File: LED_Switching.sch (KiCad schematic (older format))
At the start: 13 parts

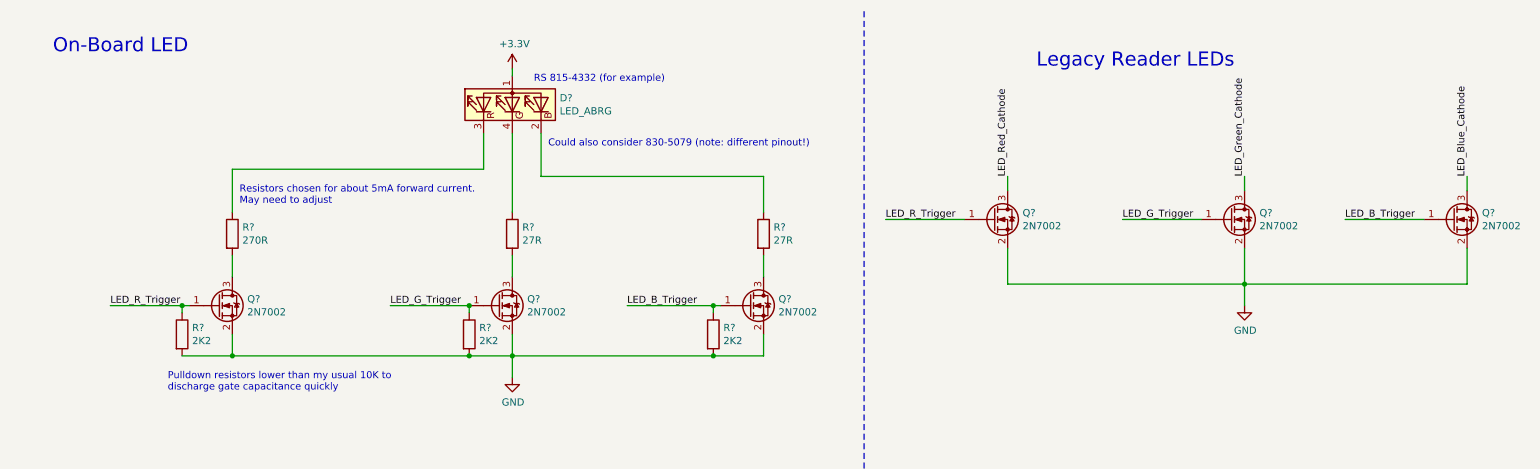
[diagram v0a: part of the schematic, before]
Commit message: Annotated some symbols and linked nets properly between sheets
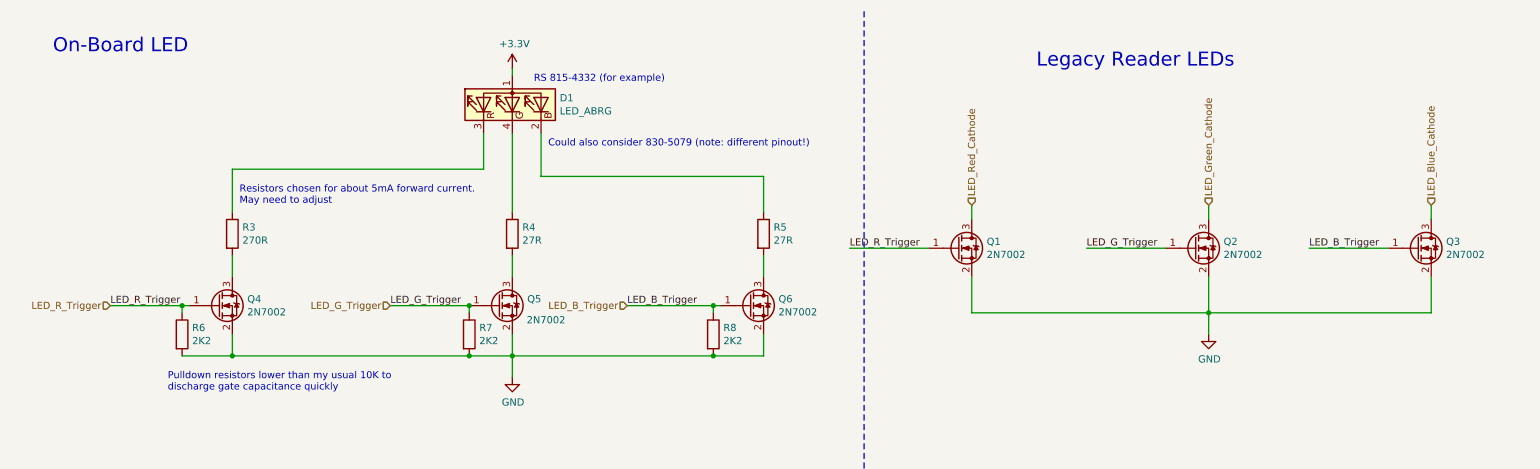
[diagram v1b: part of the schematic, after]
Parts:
- R3, R4, R5, R6, R7, R8: renamed from R?; footprint (none) -> Resistor_SMD:R_0603_1608Metric
- gave numbers to parts that had none: 7
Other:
- moved on the sheet: Q1, Q2, Q3
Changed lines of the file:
@@
 P 4050 1150
 AR Path="/5FDB67B7" Ref="D?"  Part="1"
-AR Path="/5FDAF572/5FDB67B7" Ref="D?"  Part="1"
-F 0 "D?" V 4096 820 50  0000 R CNN
+AR Path="/5FDAF572/5FDB67B7" Ref="D1"  Part="1"
+F 0 "D1" V 4096 820 50  0000 R CNN
 F 1 "LED_ABRG" V 4005 820 50  0000 R CNN
 F 2 "" H 4050 1150 50  0001 C CNN
@@
 P 4050 2050
 AR Path="/5FDCD5C9" Ref="R?"  Part="1"
-AR Path="/5FDAF572/5FDCD5C9" Ref="R?"  Part="1"
-F 0 "R?" H 4120 2096 50  0000 L CNN
+AR Path="/5FDAF572/5FDCD5C9" Ref="R4"  Part="1"
+F 0 "R4" H 4120 2096 50  0000 L CNN
 F 1 "27R" H 4120 2005 50  0000 L CNN
-F 2 "" V 3980 2050 50  0001 C CNN
+F 2 "Resistor_SMD:R_0603_1608Metric" V 3980 2050 50  0001 C CNN
 F 3 "~" H 4050 2050 50  0001 C CNN
 	1    4050 2050
@@
 P 3950 2550
 AR Path="/5FDCD5CF" Ref="Q?"  Part="1"
-AR Path="/5FDAF572/5FDCD5CF" Ref="Q?"  Part="1"
-F 0 "Q?" H 4154 2596 50  0000 L CNN
-F 1 "2N7002" H 4154 2505 50  0000 L CNN
+AR Path="/5FDAF572/5FDCD5CF" Ref="Q5"  Part="1"
+F 0 "Q5" H 4154 2596 50  0000 L CNN
+F 1 "2N7002" H 4150 2450 50  0000 L CNN
 F 2 "Package_TO_SOT_SMD:SOT-23" H 4150 2475 50  0001 L CIN
 F 3 "https://www.fairchildsemi.com/datasheets/2N/2N7002.pdf" H 3950 2550 50  0001 L CNN
@@
 P 5800 2050
 AR Path="/5FDCEFE5" Ref="R?"  Part="1"
-AR Path="/5FDAF572/5FDCEFE5" Ref="R?"  Part="1"
-F 0 "R?" H 5870 2096 50  0000 L CNN
+AR Path="/5FDAF572/5FDCEFE5" Ref="R5"  Part="1"
+F 0 "R5" H 5870 2096 50  0000 L CNN
 F 1 "27R" H 5870 2005 50  0000 L CNN
-F 2 "" V 5730 2050 50  0001 C CNN
+F 2 "Resistor_SMD:R_0603_1608Metric" V 5730 2050 50  0001 C CNN
 F 3 "~" H 5800 2050 50  0001 C CNN
 	1    5800 2050
@@
 P 5700 2550
 AR Path="/5FDCEFEB" Ref="Q?"  Part="1"
-AR Path="/5FDAF572/5FDCEFEB" Ref="Q?"  Part="1"
-F 0 "Q?" H 5904 2596 50  0000 L CNN
+AR Path="/5FDAF572/5FDCEFEB" Ref="Q6"  Part="1"
+F 0 "Q6" H 5904 2596 50  0000 L CNN
 F 1 "2N7002" H 5904 2505 50  0000 L CNN
 F 2 "Package_TO_SOT_SMD:SOT-23" H 5900 2475 50  0001 L CIN
@@
 	5800 2750 5800 2900
 $Comp
-L Transistor_FET:2N7002 Q?
+L Transistor_FET:2N7002 Q1
 U 1 1 5FDFC391
-P 7400 1950
-F 0 "Q?" H 7604 1996 50  0000 L CNN
-F 1 "2N7002" H 7604 1905 50  0000 L CNN
-F 2 "Package_TO_SOT_SMD:SOT-23" H 7600 1875 50  0001 L CIN
-F 3 "https://www.fairchildsemi.com/datasheets/2N/2N7002.pdf" H 7400 1950 50  0001 L CNN
-	1    7400 1950
-	1    0    0    -1
-$EndComp
-$Comp
-L Transistor_FET:2N7002 Q?
+P 7150 2150
+F 0 "Q1" H 7354 2196 50  0000 L CNN
+F 1 "2N7002" H 7354 2105 50  0000 L CNN
+F 2 "Package_TO_SOT_SMD:SOT-23" H 7350 2075 50  0001 L CIN
+F 3 "https://www.fairchildsemi.com/datasheets/2N/2N7002.pdf" H 7150 2150 50  0001 L CNN
+	1    7150 2150
+	1    0    0    -1
+$EndComp
+$Comp
+L Transistor_FET:2N7002 Q2
 U 1 1 5FDFF38B
-P 9050 1950
-F 0 "Q?" H 9254 1996 50  0000 L CNN
-F 1 "2N7002" H 9254 1905 50  0000 L CNN
-F 2 "Package_TO_SOT_SMD:SOT-23" H 9250 1875 50  0001 L CIN
-F 3 "https://www.fairchildsemi.com/datasheets/2N/2N7002.pdf" H 9050 1950 50  0001 L CNN
-	1    9050 1950
-	1    0    0    -1
-$EndComp
-$Comp
-L Transistor_FET:2N7002 Q?
+P 8800 2150
+F 0 "Q2" H 9004 2196 50  0000 L CNN
+F 1 "2N7002" H 9004 2105 50  0000 L CNN
+F 2 "Package_TO_SOT_SMD:SOT-23" H 9000 2075 50  0001 L CIN
+F 3 "https://www.fairchildsemi.com/datasheets/2N/2N7002.pdf" H 8800 2150 50  0001 L CNN
+	1    8800 2150
+	1    0    0    -1
+$EndComp
+$Comp
+L Transistor_FET:2N7002 Q3
 U 1 1 5FE04D0B
-P 10600 1950
-F 0 "Q?" H 10804 1996 50  0000 L CNN
-F 1 "2N7002" H 10804 1905 50  0000 L CNN
-F 2 "Package_TO_SOT_SMD:SOT-23" H 10800 1875 50  0001 L CIN
-F 3 "https://www.fairchildsemi.com/datasheets/2N/2N7002.pdf" H 10600 1950 50  0001 L CNN
-	1    10600 1950
+P 10350 2150
+F 0 "Q3" H 10554 2196 50  0000 L CNN
+F 1 "2N7002" H 10554 2105 50  0000 L CNN
+F 2 "Package_TO_SOT_SMD:SOT-23" H 10550 2075 50  0001 L CIN
+F 3 "https://www.fairchildsemi.com/datasheets/2N/2N7002.pdf" H 10350 2150 50  0001 L CNN
+	1    10350 2150
 	1    0    0    -1
 $EndComp
@@
 L power:GND #PWR0121
 U 1 1 5FE094F3
-P 9150 2550
-F 0 "#PWR0121" H 9150 2300 50  0001 C CNN
-F 1 "GND" H 9155 2377 50  0000 C CNN
-F 2 "" H 9150 2550 50  0001 C CNN
-F 3 "" H 9150 2550 50  0001 C CNN
-	1    9150 2550
+P 8900 2750
+F 0 "#PWR0121" H 8900 2500 50  0001 C CNN
+F 1 "GND" H 8905 2577 50  0000 C CNN
+F 2 "" H 8900 2750 50  0001 C CNN
+F 3 "" H 8900 2750 50  0001 C CNN
+	1    8900 2750
 	1    0    0    -1
 $EndComp
@@
 Legacy Reader LEDs
 Wire Wire Line
-	7500 2150 7500 2400
-Wire Wire Line
-	10700 2400 10700 2150
+	7250 2350 7250 2600
+Wire Wire Line
+	10450 2600 10450 2350
 Wire Wire Line
 	2100 2750 2100 2900
@@
 P 2000 2550
 AR Path="/5FDB67DA" Ref="Q?"  Part="1"
-AR Path="/5FDAF572/5FDB67DA" Ref="Q?"  Part="1"
-F 0 "Q?" H 2204 2596 50  0000 L CNN
+AR Path="/5FDAF572/5FDB67DA" Ref="Q4"  Part="1"
+F 0 "Q4" H 2204 2596 50  0000 L CNN
 F 1 "2N7002" H 2204 2505 50  0000 L CNN
 F 2 "Package_TO_SOT_SMD:SOT-23" H 2200 2475 50  0001 L CIN
@@
 P 2100 2050
 AR Path="/5FDB67BE" Ref="R?"  Part="1"
-AR Path="/5FDAF572/5FDB67BE" Ref="R?"  Part="1"
-F 0 "R?" H 2170 2096 50  0000 L CNN
+AR Path="/5FDAF572/5FDB67BE" Ref="R3"  Part="1"
+F 0 "R3" H 2170 2096 50  0000 L CNN
 F 1 "270R" H 2170 2005 50  0000 L CNN
-F 2 "" V 2030 2050 50  0001 C CNN
+F 2 "Resistor_SMD:R_0603_1608Metric" V 2030 2050 50  0001 C CNN
 F 3 "~" H 2100 2050 50  0001 C CNN
 	1    2100 2050
@@
 Wire Wire Line
 	5500 2550 5450 2550
-Text Label 7500 1650 1    49   ~ 0
-LED_Red_Cathode
-Text Label 9150 1650 1    49   ~ 0
-LED_Green_Cathode
-Text Label 10700 1650 1    49   ~ 0
-LED_Blue_Cathode
-Wire Wire Line
-	10700 1750 10700 1650
-Wire Wire Line
-	9150 1750 9150 1650
-Wire Wire Line
-	7500 1750 7500 1650
-Text Label 6650 1950 0    49   ~ 0
+Wire Wire Line
+	10450 1950 10450 1850
+Wire Wire Line
+	8900 1950 8900 1850
+Wire Wire Line
+	7250 1950 7250 1850
+Text Label 6400 2150 0    49   ~ 0
 LED_R_Trigger
-Text Label 8300 1950 0    49   ~ 0
+Text Label 8050 2150 0    49   ~ 0
 LED_G_Trigger
-Text Label 9850 1950 0    49   ~ 0
+Text Label 9600 2150 0    49   ~ 0
 LED_B_Trigger
 Wire Wire Line
-	9150 2150 9150 2400
-Wire Wire Line
-	10700 2400 9150 2400
-Connection ~ 9150 2400
-Wire Wire Line
-	9150 2400 9150 2550
-Wire Wire Line
-	9150 2400 7500 2400
-Wire Wire Line
-	10400 1950 9850 1950
-Wire Wire Line
-	8850 1950 8300 1950
-Wire Wire Line
-	7200 1950 6650 1950
-$Comp
-L Device:R R?
+	8900 2350 8900 2600
+Wire Wire Line
+	10450 2600 8900 2600
+Connection ~ 8900 2600
+Wire Wire Line
+	8900 2600 8900 2750
+Wire Wire Line
+	8900 2600 7250 2600
+Wire Wire Line
+	10150 2150 9600 2150
+Wire Wire Line
+	8600 2150 8050 2150
+Wire Wire Line
+	6950 2150 6400 2150
+$Comp
+L Device:R R6
 U 1 1 5FF0DB90
 P 1750 2750
-F 0 "R?" H 1820 2796 50  0000 L CNN
+F 0 "R6" H 1820 2796 50  0000 L CNN
 F 1 "2K2" H 1820 2705 50  0000 L CNN
-F 2 "" V 1680 2750 50  0001 C CNN
+F 2 "Resistor_SMD:R_0603_1608Metric" V 1680 2750 50  0001 C CNN
 F 3 "~" H 1750 2750 50  0001 C CNN
 	1    1750 2750
@@
 	1750 2550 1250 2550
 $Comp
-L Device:R R?
+L Device:R R7
 U 1 1 5FF11CB4
 P 3750 2750
-F 0 "R?" H 3820 2796 50  0000 L CNN
+F 0 "R7" H 3820 2796 50  0000 L CNN
 F 1 "2K2" H 3820 2705 50  0000 L CNN
-F 2 "" V 3680 2750 50  0001 C CNN
+F 2 "Resistor_SMD:R_0603_1608Metric" V 3680 2750 50  0001 C CNN
 F 3 "~" H 3750 2750 50  0001 C CNN
 	1    3750 2750
@@
 Connection ~ 3750 2550
 $Comp
-L Device:R R?
+L Device:R R8
 U 1 1 5FF13B9B
 P 5450 2750
-F 0 "R?" H 5520 2796 50  0000 L CNN
+F 0 "R8" H 5520 2796 50  0000 L CNN
 F 1 "2K2" H 5520 2705 50  0000 L CNN
-F 2 "" V 5380 2750 50  0001 C CNN
+F 2 "Resistor_SMD:R_0603_1608Metric" V 5380 2750 50  0001 C CNN
 F 3 "~" H 5450 2750 50  0001 C CNN
 	1    5450 2750
@@
 Text Notes 2150 1850 0    49   ~ 0
 Resistors chosen for about 5mA forward current.\nMay need to adjust
+Text HLabel 1250 2550 0    49   Input ~ 0
+LED_R_Trigger
+Text HLabel 3200 2550 0    49   Input ~ 0
+LED_G_Trigger
+Text HLabel 4850 2550 0    49   Input ~ 0
+LED_B_Trigger
+Text HLabel 7250 1850 1    49   Input ~ 0
+LED_Red_Cathode
+Text HLabel 8900 1850 1    49   Input ~ 0
+LED_Green_Cathode
+Text HLabel 10450 1850 1    49   Input ~ 0
+LED_Blue_Cathode
 $EndSCHEMATC

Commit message: First pass at routing board fully
Also fixed a stupid error on the Nucleo-144 footprint
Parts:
- D1: footprint (none) -> ExtraParts:Wurth_3528_LED
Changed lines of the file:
@@
 F 0 "D1" V 4096 820 50  0000 R CNN
 F 1 "LED_ABRG" V 4005 820 50  0000 R CNN
-F 2 "" H 4050 1150 50  0001 C CNN
-F 3 "~" H 4050 1150 50  0001 C CNN
+F 2 "ExtraParts:Wurth_3528_LED" H 4050 1150 50  0001 C CNN
+F 3 "https://www.we-online.de/katalog/datasheet/150141M173100.pdf" H 4050 1150 50  0001 C CNN
 	1    4050 1150
 	0    -1   -1   0
